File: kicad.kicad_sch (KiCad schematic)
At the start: 22 parts, among them J1 Screw_Terminal_01x02, J2 Screw_Terminal_01x03, J3 Screw_Terminal_01x03, J4 Screw_Terminal_01x03, J5 Conn_01x03, J6 ICSP, J7 Conn_01x05, SW1 SW_Push, SW2 SW_Push, U1 DS1233A-10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

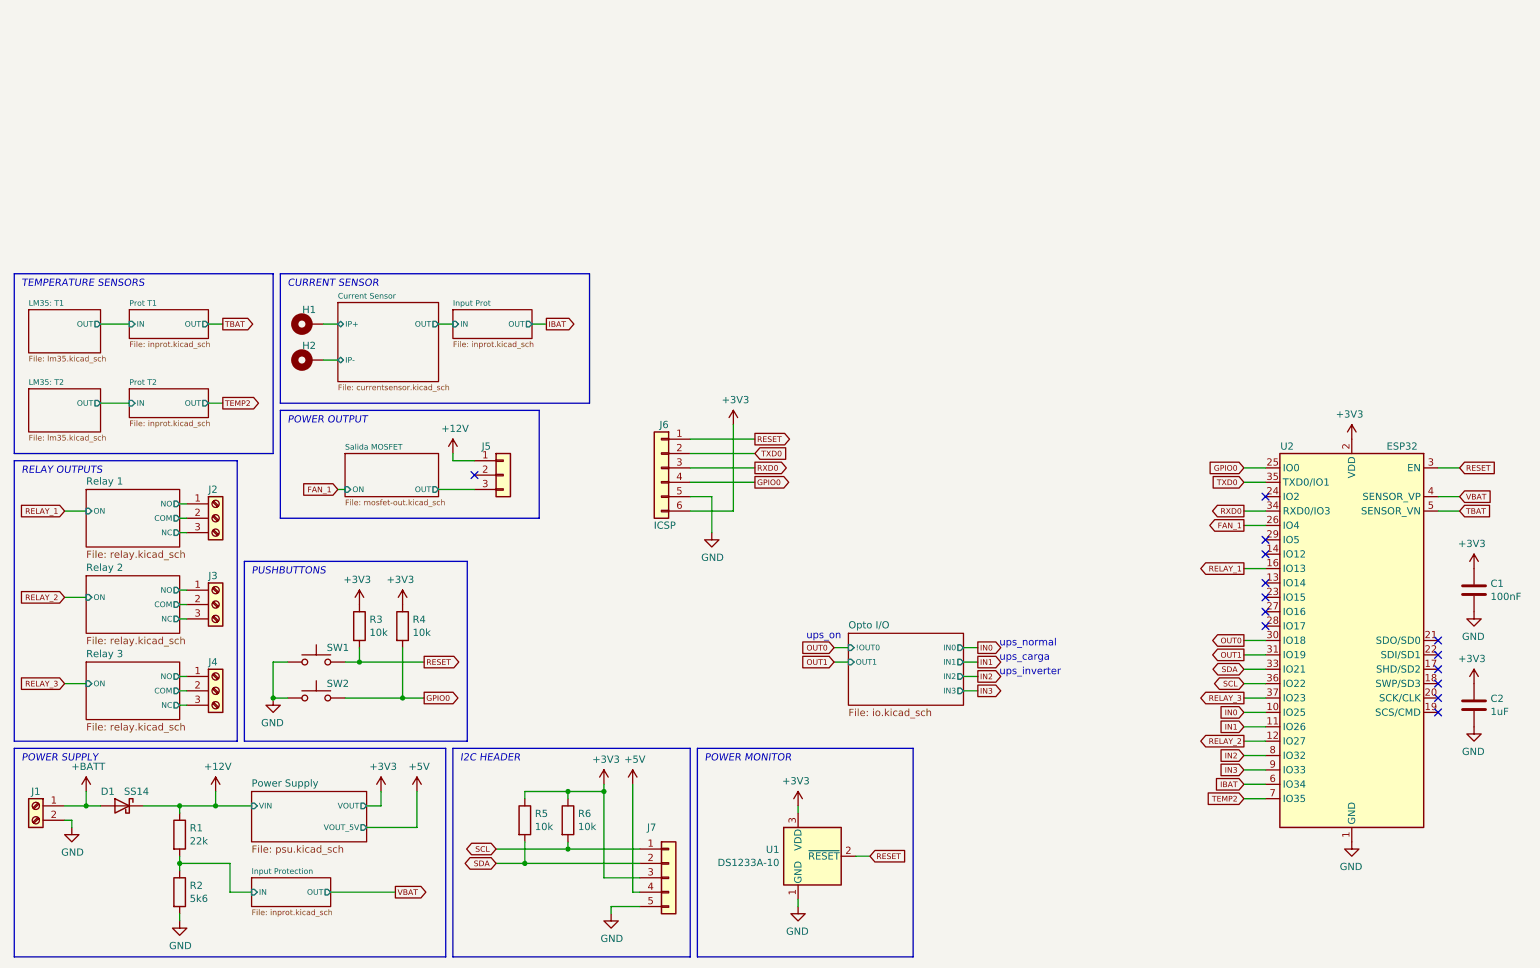
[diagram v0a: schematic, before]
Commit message: Move tp doc file
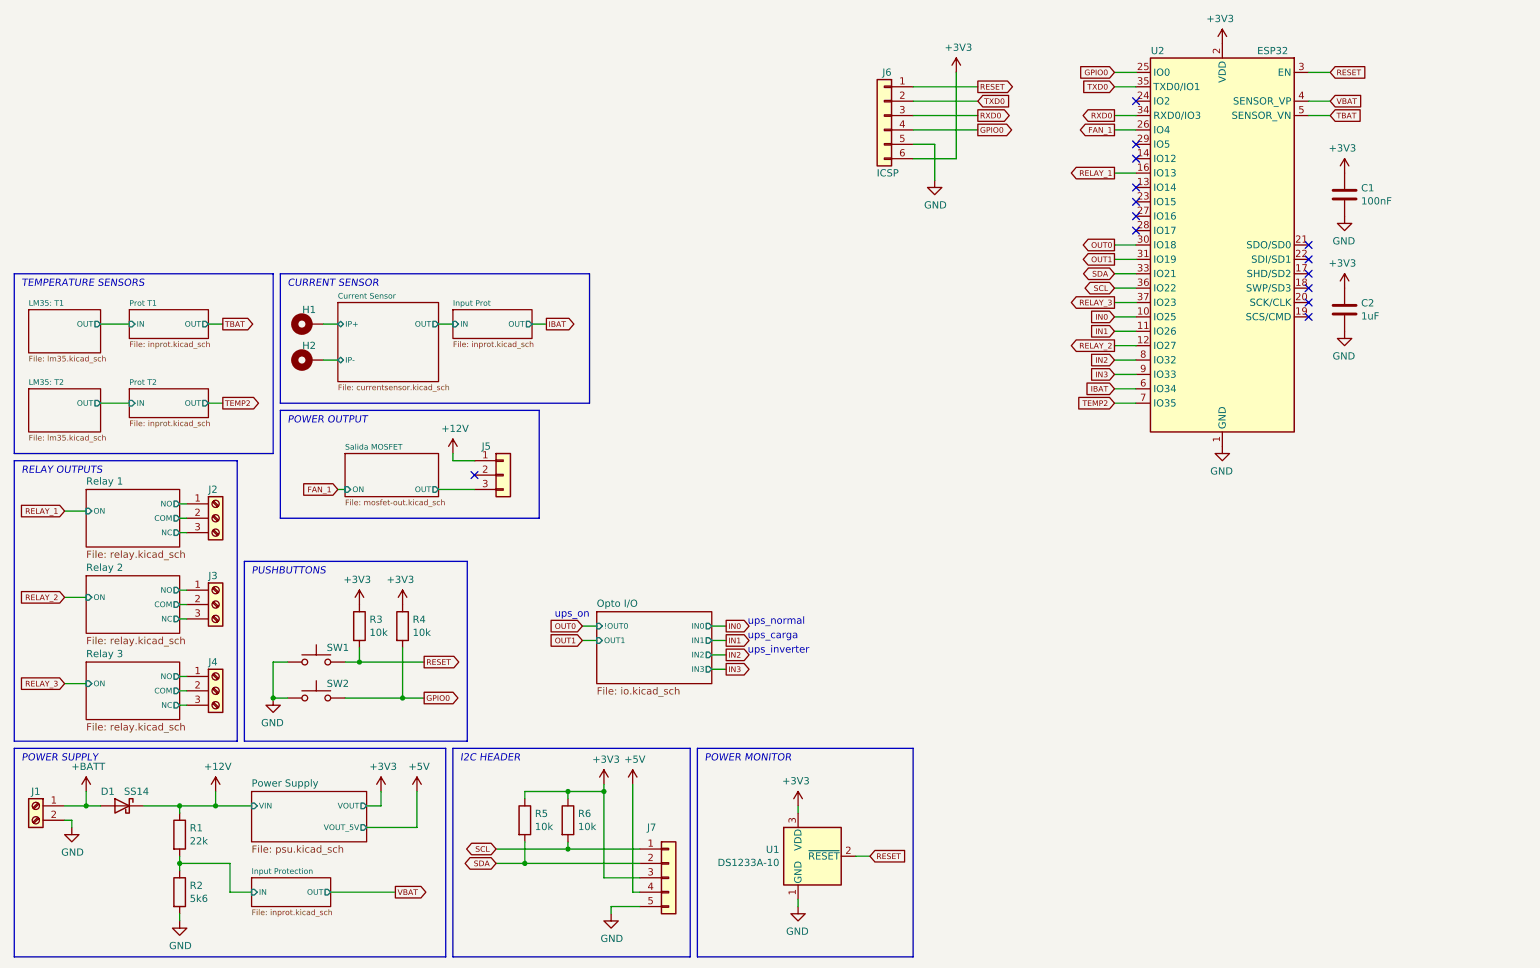
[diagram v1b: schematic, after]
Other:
- title: ESP32 Uninterrupted Power Supply Monitor -> ESP32-PLC
- moved on the sheet: C1, C2, J6, U2
